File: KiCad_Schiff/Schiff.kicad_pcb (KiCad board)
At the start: 2 copper layers, 150 x 60 mm, 28 parts, among them J1 Conn_01x02, J2 L298N, J3 AMS1117-Module, J4 L298N, J5 Screw_Terminal_01x02, J6 Screw_Terminal_01x02, M1 Motor_Servo, M2 Motor_Servo, M3 Motor_Servo, SW1 SW_Wuerth_450301014042, SW2 SW_Wuerth_450301014042, U1 NRF24L01_Breakout

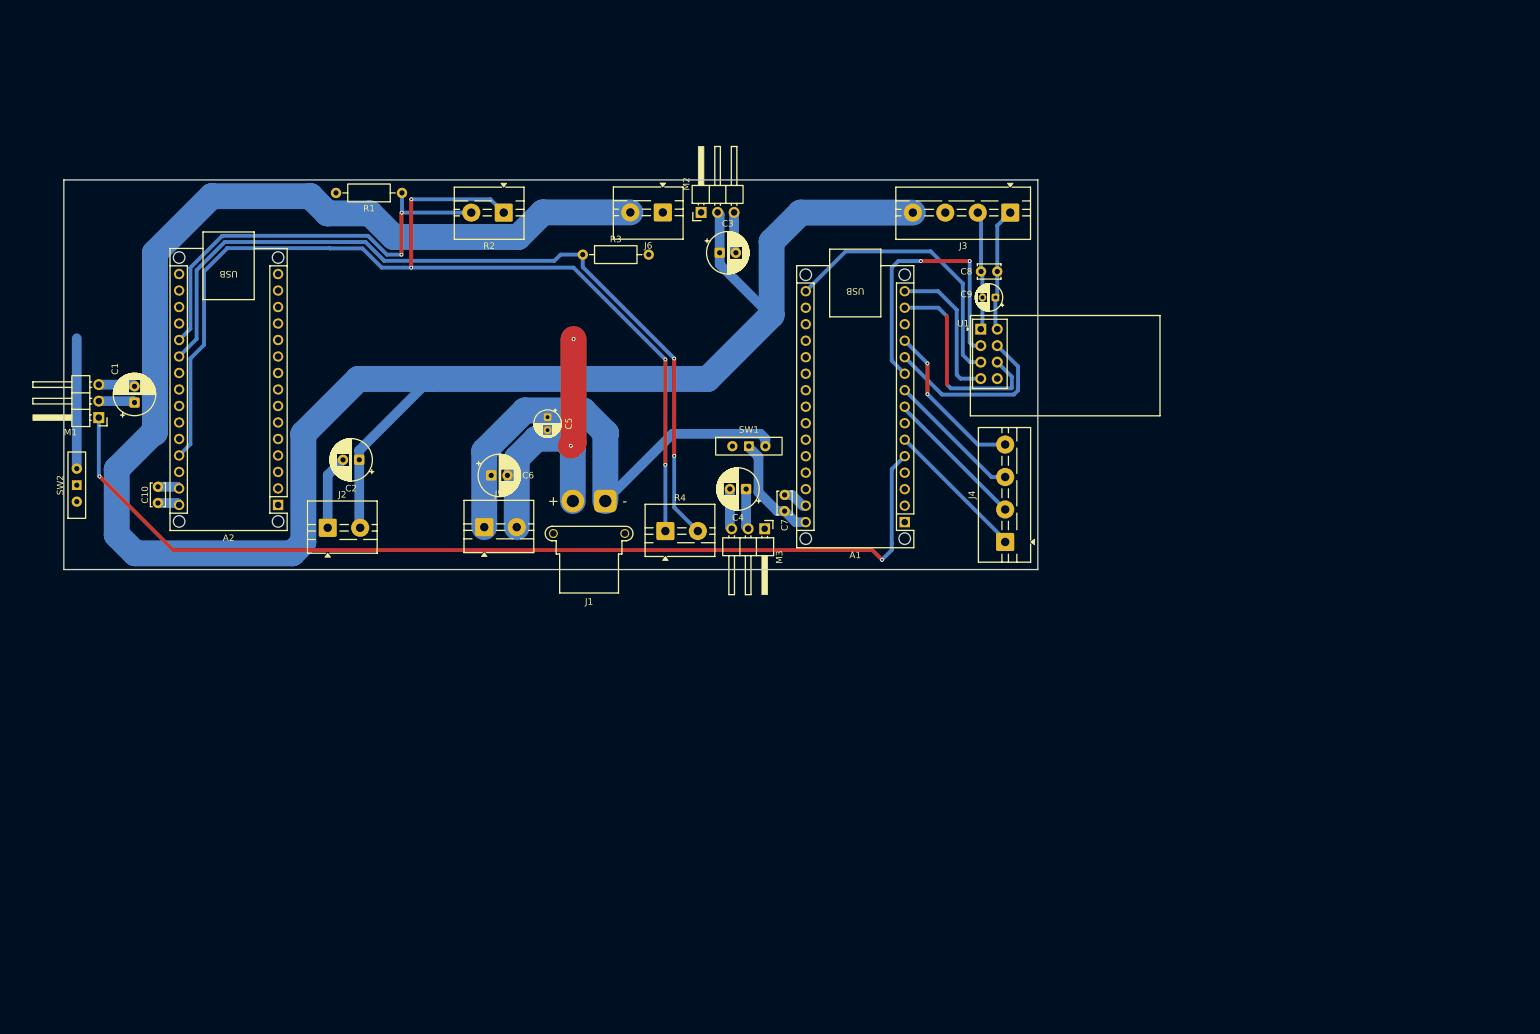
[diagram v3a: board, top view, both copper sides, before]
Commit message: Changed footprints
Changed footprints to match the given bore sizes
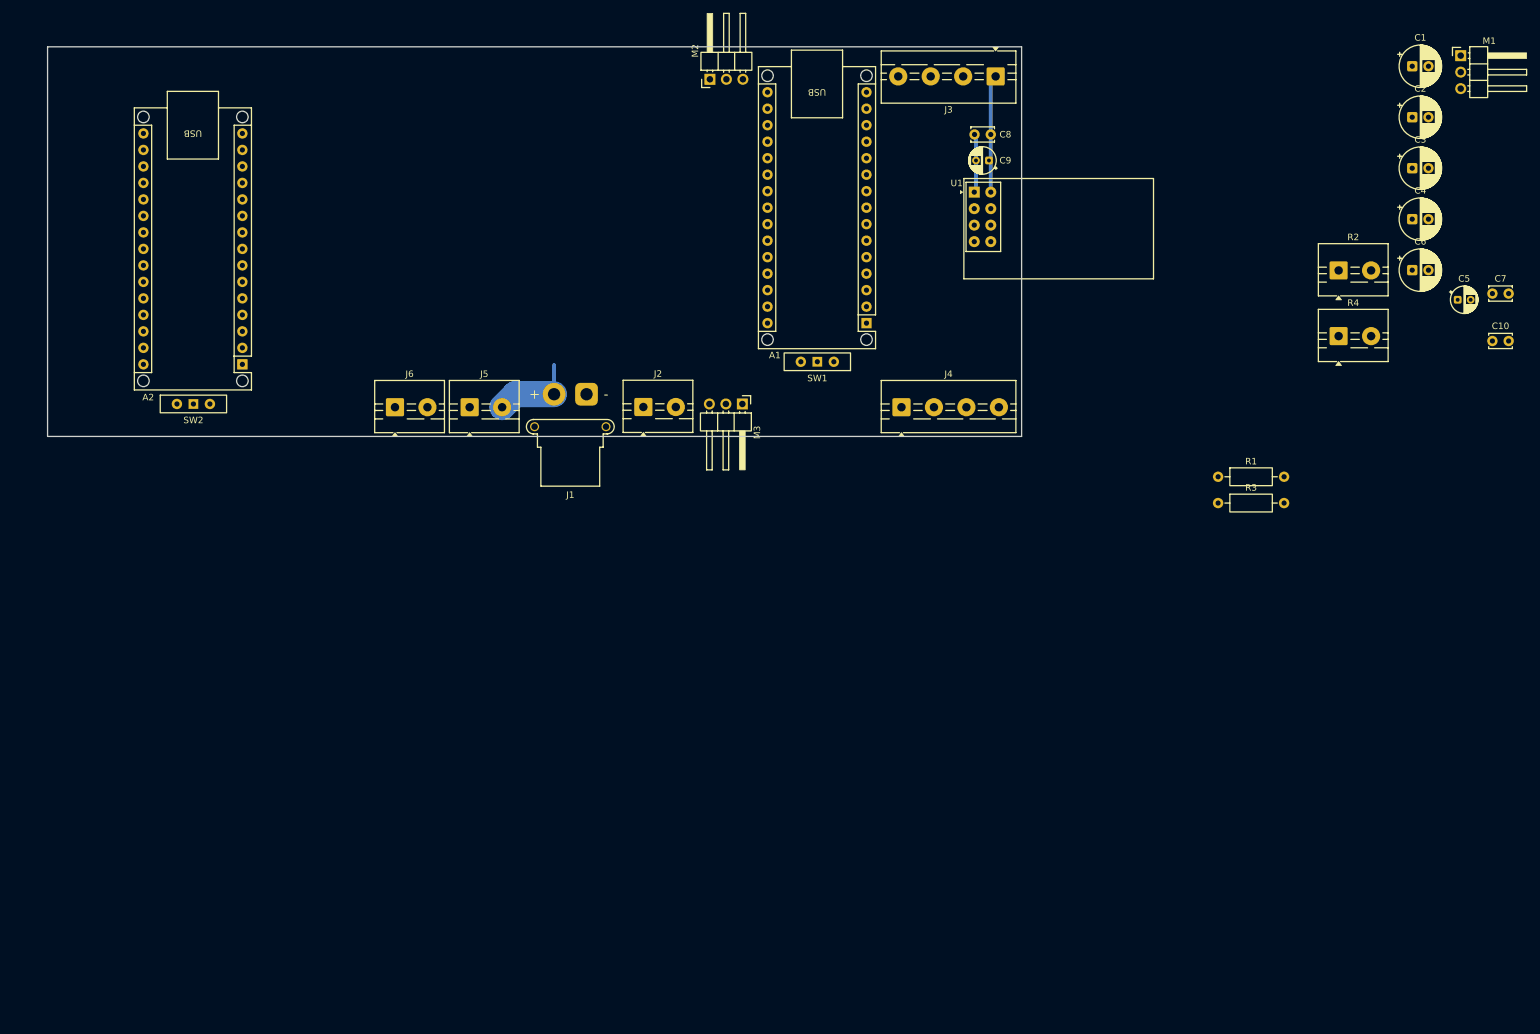
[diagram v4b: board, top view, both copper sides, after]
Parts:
- moved M1 217.0 mm to (235.6, 19.4), turned to 0 degrees
- moved C10 206.7 mm to (240.5, 63.3), turned to 0 degrees
- moved C1 203.5 mm to (228.2, 21.0), turned to 0 degrees
- moved C2 170.5 mm to (228.2, 28.8), turned to 0 degrees
- moved C6 145.3 mm to (228.2, 52.4)
- moved C5 141.3 mm to (235.2, 57.0), turned to 0 degrees
- moved R1 133.1 mm to (198.3, 84.2), turned to 0 degrees
- moved R2 128.9 mm to (216.8, 52.4), turned to 0 degrees
- moved C7 113.3 mm to (240.5, 56.0), turned to 0 degrees
- moved C4 110.7 mm to (228.2, 44.5), turned to 0 degrees
- moved R4 107.9 mm to (216.8, 62.5)
- moved C3 107.4 mm to (228.2, 36.7)
- moved R3 105.1 mm to (198.3, 88.3)
- moved J2 52.0 mm to (109.8, 73.5)
- moved J6 51.0 mm to (71.5, 73.5), turned to 0 degrees
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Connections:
- J1 pad 1: VCC_BT -> GND
- J1 pad 2: GND -> VCC_BT
- J5 pad 1: VCC_BT -> GND
- J5 pad 2: GND -> VCC_BT
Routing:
- net +5V: track 347.8 -> 0.00 mm
- net Net-(A2-+5V): track 161.6 -> 0.00 mm, vias 4 -> 0
- net /ServoStear: track 152.3 -> 0.00 mm, vias 2 -> 0
- net Net-(A2-A2): track 127.2 -> 0.00 mm, vias 2 -> 0
- net GND: track 101.1 -> 9.08 mm, vias 2 -> 0
- net VCC_BT: track 95.5 -> 13.3 mm
- net Net-(A2-A1): track 67.9 -> 0.00 mm, vias 2 -> 0
- net Net-(A1-D7): track 44.0 -> 0.00 mm, vias 2 -> 0
- net Net-(A1-D13): track 43.0 -> 0.00 mm
- net Net-(A1-D11): track 32.7 -> 0.00 mm
- net Net-(A1-D8): track 28.3 -> 0.00 mm
- net /IN4: track 24.9 -> 0.00 mm, vias 2 -> 0
- net Net-(A1-D12): track 23.1 -> 0.00 mm
- net /IN2: track 22.2 -> 0.00 mm
- net /IN1: track 22.2 -> 0.00 mm
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
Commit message: New layout for hydrofoil
This layout needs to be checked, a specially in terms of ground connections and the width of these connections
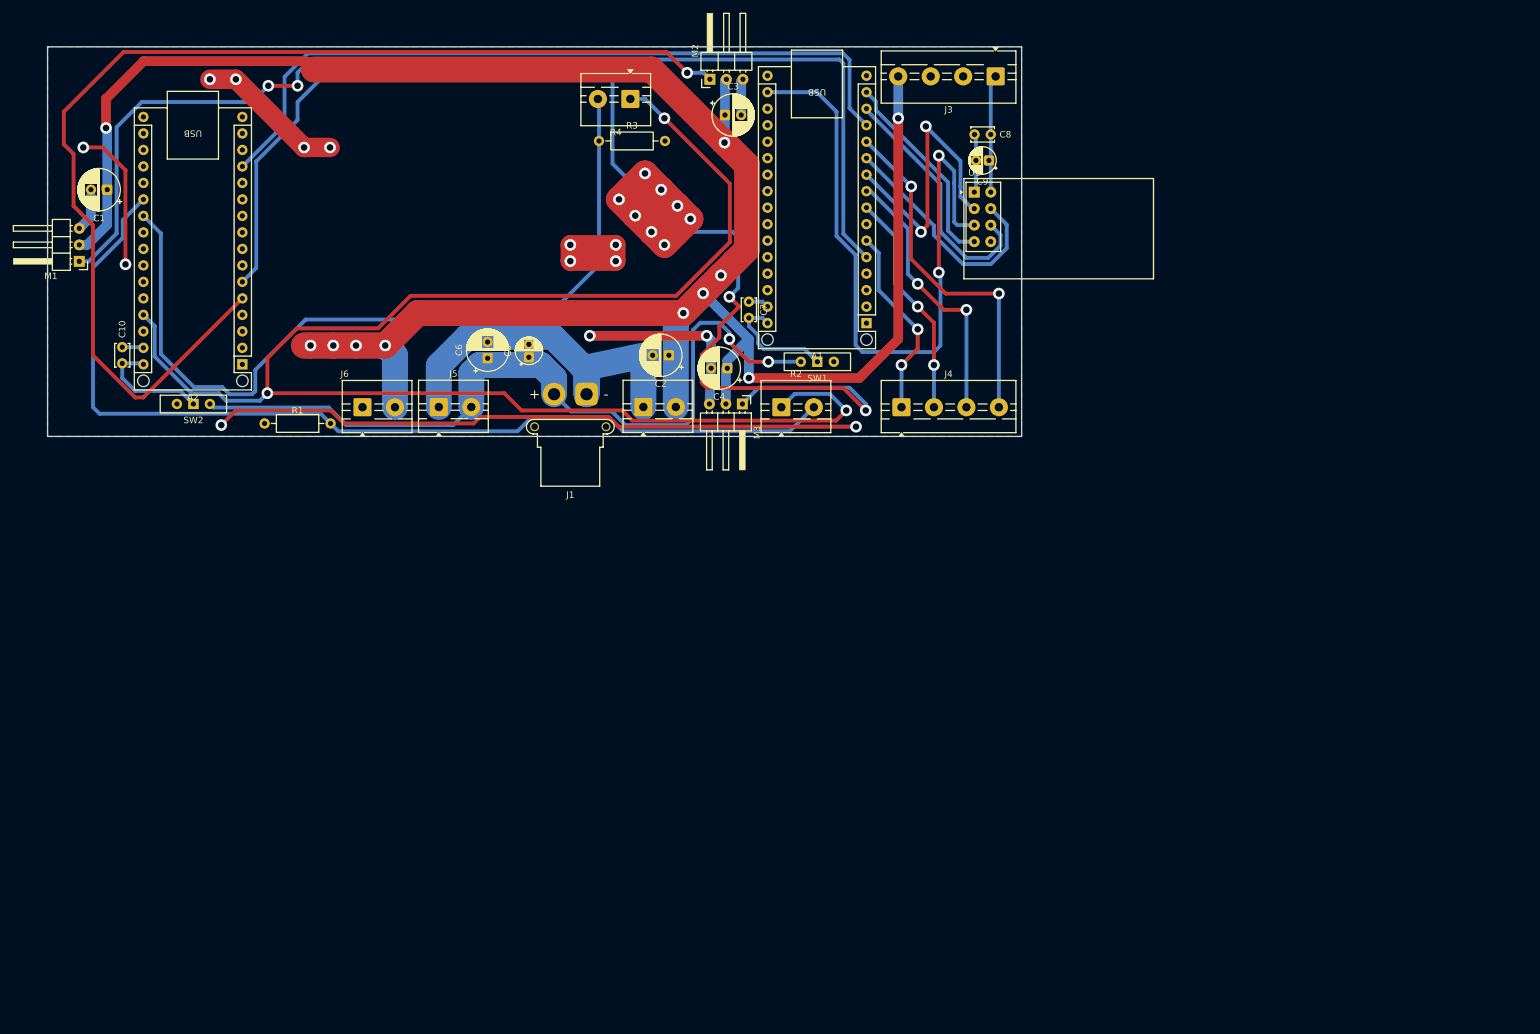
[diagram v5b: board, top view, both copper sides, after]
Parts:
- A1, A2: footprint Module:Arduino_Nano_WithMountingHoles -> LibraryNewHoleSize:Arduino_Nano_WithMountingHoles
- C5, C9: footprint Capacitor_THT:CP_Radial_D4.0mm_P2.00mm -> LibraryNewHoleSize:CP_Radial_D4.0mm_P2.00mm
- M1, M2, M3: footprint Connector_PinHeader_2.54mm:PinHeader_1x03_P2.54mm_Horizontal -> LibraryNewHoleSize:PinHeader_1x03_P2.54mm_Horizontal
- U1: footprint RF_Module:nRF24L01_Breakout -> LibraryNewHoleSize:nRF24L01_Breakout
- moved M1 215.1 mm to (22.9, 51.0), turned to 180 degrees
- moved C10 211.0 mm to (29.5, 64.2), turned to -90 degrees
- moved C1 201.9 mm to (27.2, 40.0), turned to 180 degrees
- moved C5 143.3 mm to (92.1, 65.8), turned to 90 degrees
- moved C6 143.0 mm to (85.8, 66.0), turned to 90 degrees
- moved R1 136.9 mm to (61.6, 76.0), turned to 180 degrees
- moved C2 120.2 mm to (113.7, 65.5), turned to 180 degrees
- moved R4 115.0 mm to (107.8, 26.0), turned to 180 degrees
- moved C7 114.5 mm to (126.0, 57.2), turned to -90 degrees
- moved R3 110.4 mm to (102.9, 32.5)
- moved C4 107.9 mm to (122.7, 67.5), turned to 180 degrees
- moved C3 106.2 mm to (122.3, 28.5)
- moved R2 88.4 mm to (131.0, 73.5)
- moved J6 5.00 mm to (66.5, 73.5)
- moved J5 4.75 mm to (78.2, 73.5)
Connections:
- A1 pad 29: GND -> /GND_A1
- A2 pad 29: GND -> /GND_A2
- C1 pad 2: GND -> /GND_PLANE
- C10 pad 1: GND -> /GND_PLANE
- C2 pad 2: GND -> /GND_Driver
- C3 pad 2: GND -> /GND_PLANE
- C4 pad 2: GND -> /GND_PLANE
- C5 pad 2: GND -> /GND_XL4015
- C6 pad 2: GND -> /GND_PLANE
- C7 pad 1: GND -> /GND_PLANE
- C8 pad 2: GND -> /GND_PLANE
- C9 pad 2: GND -> /GND_NRF
- J1 pad 1: GND -> /GND_PLANE
- J2 pad 1: GND -> /GND_Driver
- J3 pad 2: GND -> /GND_PLANE
- J3 pad 3: GND -> /GND_PLANE
- J5 pad 1: GND -> /GND_XL4015
- J6 pad 1: GND -> /GND_PLANE
- M1 pad 3: GND -> /GND_M1
- M2 pad 3: GND -> /GND_M2
- M3 pad 3: GND -> /GND_M3
- R1 pad 2: GND -> /GND_PLANE
- R3 pad 2: GND -> /GND_PLANE
- U1 pad 1: GND -> /GND_NRF
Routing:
- net +5V: track 0.00 -> 370.0 mm, vias 0 -> 11
- net /GND_PLANE: track 0.00 -> 250.2 mm, vias 0 -> 22
- net Net-(A2-+5V): track 0.00 -> 245.0 mm, vias 0 -> 3
- net /ServoFoilR: track 0.00 -> 196.1 mm, vias 0 -> 2
- net /ServoFoilL: track 0.00 -> 176.4 mm, vias 0 -> 1
- net /ServoStear: track 0.00 -> 172.9 mm, vias 0 -> 2
- net Net-(A2-A1): track 0.00 -> 151.0 mm
- net Net-(A2-A2): track 0.00 -> 128.2 mm
- net VCC_BT: track 13.3 -> 129.9 mm, vias 0 -> 2
- net /Arduino_Com: track 0.00 -> 116.6 mm
- net Net-(A1-D13): track 0.00 -> 107.2 mm, vias 0 -> 2
- net /IN4: track 0.00 -> 54.2 mm, vias 0 -> 2
- net Net-(A1-D7): track 0.00 -> 45.3 mm, vias 0 -> 2
- net /IN3: track 0.00 -> 42.4 mm, vias 0 -> 2
- net Net-(A1-D11): track 0.00 -> 39.2 mm
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- added copper zone on B.Cu, net /GND_PLANE

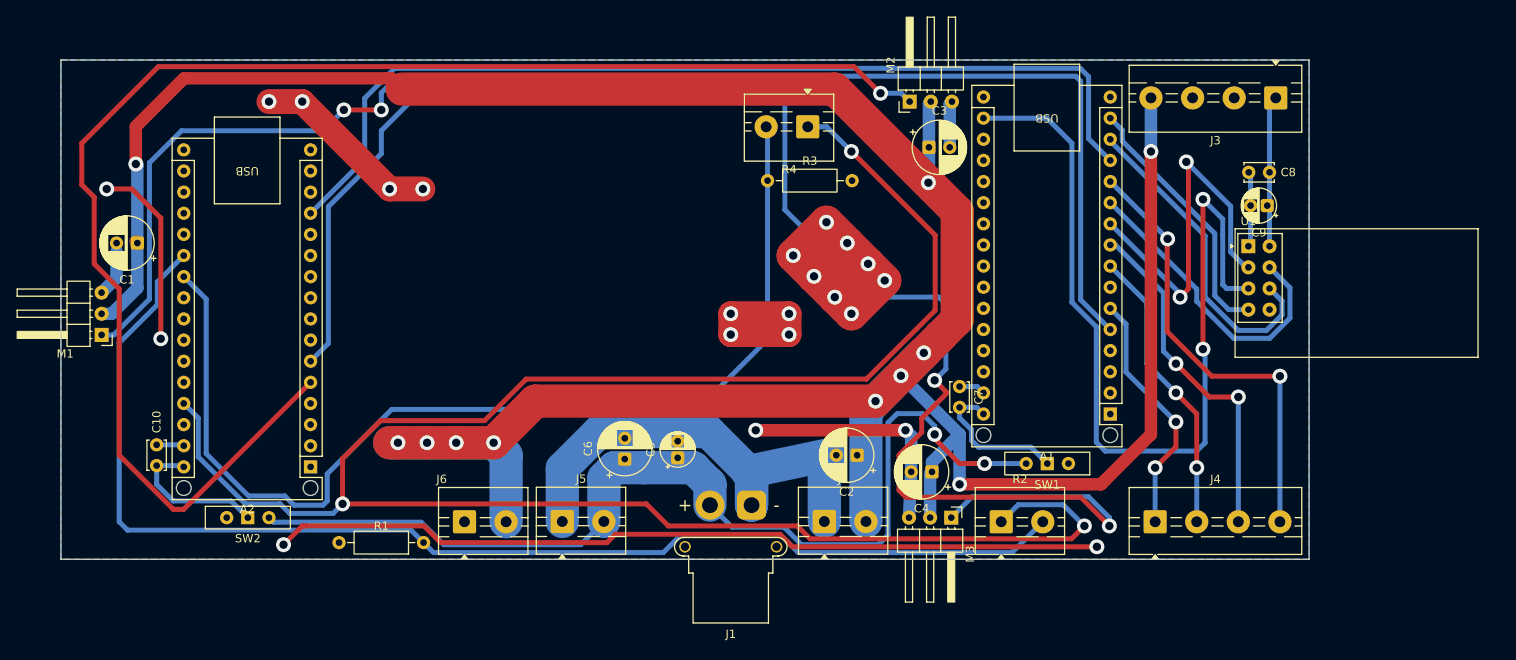
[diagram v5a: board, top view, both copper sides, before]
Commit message: New optimized PCB for foil
New PCB, with seemingly working ground-plane (the ground-plane still needs thorough review)
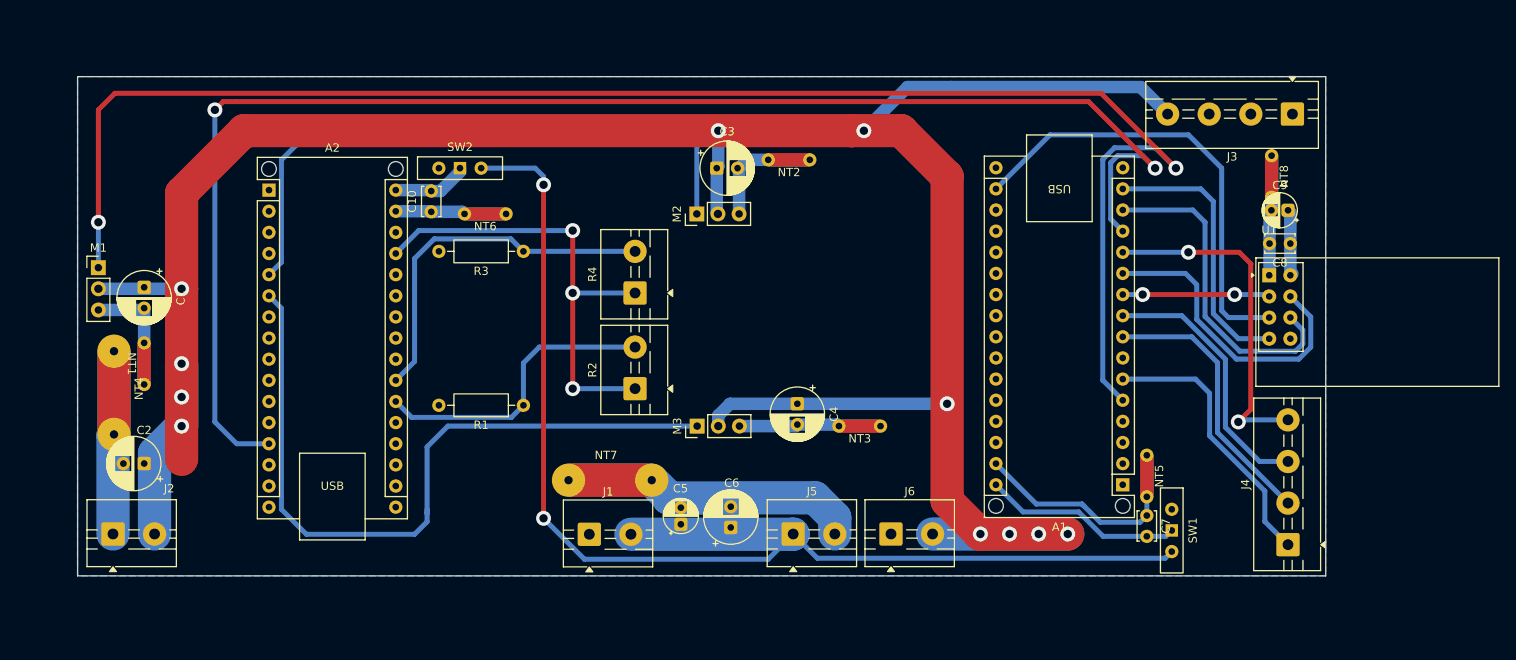
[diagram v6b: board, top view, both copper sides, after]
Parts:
- added NT1: NetTie_2, LibraryNewHoleSize:NetTie_1.6mm, F.Cu at (21.0, 55.5)
- added NT2: NetTie_2, LibraryNewHoleSize:NetTie_1.6mm, F.Cu at (106.5, 37.0)
- added NT3: NetTie_2, LibraryNewHoleSize:NetTie_1.6mm, F.Cu at (115.0, 69.0)
- added NT4: NetTie_2, LibraryNewHoleSize:NetTie_4mm, F.Cu at (31.4, 57.0)
- added NT5: NetTie_2, LibraryNewHoleSize:NetTie_1.6mm, F.Cu at (155.5, 67.0)
- added NT6: NetTie_2, LibraryNewHoleSize:NetTie_1.6mm, F.Cu at (70.0, 43.5)
- added NT7: NetTie_2, LibraryNewHoleSize:NetTie_4mm, F.Cu at (83.0, 61.5)
- added NT8: NetTie_2, LibraryNewHoleSize:NetTie_1.6mm, F.Cu at (170.5, 31.0)
- J1: footprint Connector_AMASS:AMASS_XT30PW-F_1x02_P2.50mm_Horizontal -> TerminalBlock:TerminalBlock_MaiXu_MX126-5.0-02P_1x02_P5.00mm
- M1, M2, M3: footprint LibraryNewHoleSize:PinHeader_1x03_P2.54mm_Horizontal -> LibraryNewHoleSize:PinHeader_1x03_P2.54mm_Vertical
- moved C2 85.7 mm to (28.0, 66.5)
- moved J2 85.5 mm to (24.2, 75.0)
- moved J6 51.3 mm to (117.8, 75.0)
- moved SW2 49.1 mm to (66.0, 31.0)
- moved R2 46.8 mm to (87.0, 57.5), turned to 90 degrees
- moved C10 43.3 mm to (62.5, 36.2), turned to 90 degrees
- moved A2 33.6 mm to (43.0, 33.6), turned to 0 degrees
- moved M3 32.5 mm to (94.5, 62.0), turned to 90 degrees
- moved R3 30.5 mm to (73.6, 41.0), turned to 180 degrees
- moved M2 28.9 mm to (94.4, 36.5)
- moved R4 28.8 mm to (87.0, 46.0), turned to 90 degrees
- moved J5 27.8 mm to (106.0, 75.0)
- moved C7 27.3 mm to (148.5, 72.8)
- moved C3 25.6 mm to (96.8, 31.0)
- moved R1 20.4 mm to (73.6, 59.5)
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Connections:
- C1 pad 2: /GND_PLANE -> /GND_M1
- C10 pad 1: /GND_PLANE -> /GND_A2
- C3 pad 2: /GND_PLANE -> /GND_M2
- C4 pad 2: /GND_PLANE -> /GND_M3
- C6 pad 2: /GND_PLANE -> /GND_XL4015
- C7 pad 1: /GND_PLANE -> /GND_A1
- C8 pad 2: /GND_PLANE -> /GND_NRF
- J5 pad 1: /GND_XL4015 -> VCC_BT
- J5 pad 2: VCC_BT -> /GND_XL4015
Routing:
- net /GND_PLANE: track 250.2 -> 0.00 mm, vias 22 -> 0
- net Net-(A2-+5V): track 245.0 -> 56.4 mm
- net Net-(A2-A1): track 151.0 -> 36.0 mm
- net /ServoFoilR: track 196.1 -> 88.6 mm, vias 2 -> 0
- net /ServoFoilL: track 176.4 -> 76.4 mm, vias 1 -> 0
- net Net-(A2-A2): track 128.2 -> 43.7 mm
- net /Arduino_Com: track 116.6 -> 177.0 mm, vias 0 -> 2
- net +5V: track 370.0 -> 312.3 mm
- net Net-(A1-D13): track 107.2 -> 54.7 mm, vias 2 -> 0
- net Net-(A1-D7): track 45.3 -> 17.7 mm
- net /GND_XL4015: track 0.00 -> 26.0 mm
- net /ServoStear: track 172.9 -> 193.3 mm
- net VCC_BT: track 129.9 -> 148.9 mm
- net /IN4: track 54.2 -> 41.7 mm
- net /GND_M3: track 0.11 -> 12.1 mm
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
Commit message: final PCB with mounting holes
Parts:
- added H1: MountingHole, MountingHole:MountingHole_3.2mm_M3, F.Cu at (160.0, 32.5)
- added H2: MountingHole, MountingHole:MountingHole_3.2mm_M3, F.Cu at (157.0, 75.0)
- added H3: MountingHole, MountingHole:MountingHole_3.2mm_M3, F.Cu at (27.0, 27.0)
- added H4: MountingHole, MountingHole:MountingHole_3.2mm_M3, F.Cu at (37.0, 75.0)
- moved NT7 3.38 mm to (83.0, 58.1)
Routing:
- net VCC: track 9.09 -> 20.1 mm
- net /GND_PLANE: track 0.00 -> 5.00 mm
- net +5V: track 312.3 -> 307.3 mm
- net /GND_XL4015: track 26.0 -> 29.3 mm
- net VCC_BT: track 148.9 -> 149.7 mm
- net /ServoFoilR: track 88.6 -> 88.1 mm
